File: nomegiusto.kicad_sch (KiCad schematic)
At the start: 14 parts, among them CN1 Wago connector, CN2 Wago connector, CN3 Wago connector, CN4 Wago connector, CN5 Wago connector, CN6 Wago connector, J20 Conn_01x03, J21 Conn_01x03

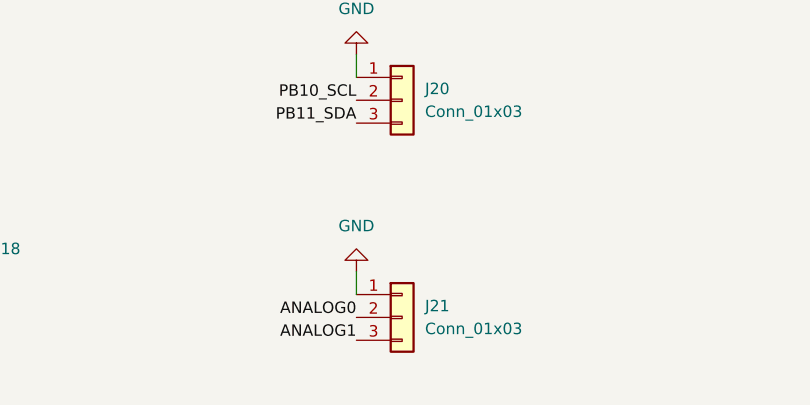
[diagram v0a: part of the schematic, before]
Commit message: changed IMU, reworked PCB layout
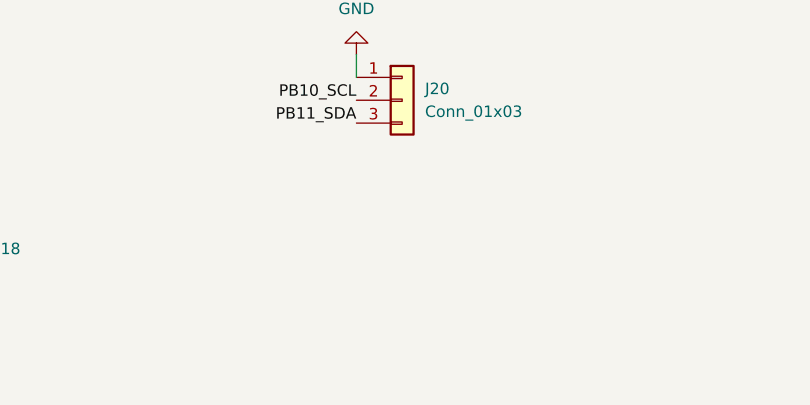
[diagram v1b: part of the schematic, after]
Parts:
- removed J21: Conn_01x03, Connector_PinHeader_2.54mm:PinHeader_1x03_P2.54mm_Vertical, symbol Connector_Generic:Conn_01x03
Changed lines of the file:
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@@
-	(wire
-		(pts
-			(xy 106.68 140.97) (xy 106.68 143.51)
-		)
-		(stroke
-			(width 0)
-			(type default)
-		)
-	)
 	(wire
 		(pts
@@
 		)
 	)
-	(label "ANALOG0"
-		(at 106.68 146.05 180)
-		(effects
-			(font
-				(size 1.27 1.27)
-			)
-			(justify right bottom)
-		)
-	)
 	(label "INPUT6"
 		(at 105.41 52.07 180)
@@
 	(label "PB11_SDA"
 		(at 106.68 124.46 180)
-		(effects
-			(font
-				(size 1.27 1.27)
-			)
-			(justify right bottom)
-		)
-	)
-	(label "ANALOG1"
-		(at 106.68 148.59 180)
 		(effects
 			(font
@@
 					(unit 1)
 				)
-			)
-		)
-	)
-	(symbol
-		(lib_id "power:GND")
-		(at 106.68 140.97 180)
-		(unit 1)
-		(body_style 1)
-		(exclude_from_sim no)
-		(in_bom yes)
-		(on_board yes)
-		(in_pos_files yes)
-		(dnp no)
-		(fields_autoplaced yes)
-		(property "Reference" "#PWR092"
-			(at 106.68 134.62 0)
-			(hide yes)
-			(show_name no)
-			(do_not_autoplace no)
-			(effects
-				(font
-					(size 1.27 1.27)
-				)
-			)
-		)
-		(property "Value" "GND"
-			(at 106.68 135.89 0)
-			(show_name no)
-			(do_not_autoplace no)
-			(effects
-				(font
-					(size 1.27 1.27)
-				)
-			)
-		)
-		(property "Footprint" ""
-			(at 106.68 140.97 0)
-			(hide yes)
-			(show_name no)
-			(do_not_autoplace no)
-			(effects
-				(font
-					(size 1.27 1.27)
-				)
-			)
-		)
-		(property "Datasheet" ""
-			(at 106.68 140.97 0)
-			(hide yes)
-			(show_name no)
-			(do_not_autoplace no)
-			(effects
-				(font
-					(size 1.27 1.27)
-				)
-			)
-		)
-		(property "Description" "Power symbol creates a global label with name \"GND\" , ground"
-			(at 106.68 140.97 0)
-			(hide yes)
-			(show_name no)
-			(do_not_autoplace no)
-			(effects
-				(font
-					(size 1.27 1.27)
-				)
-			)
-		)
-		(pin "1"
-		)
-		(instances
-			(project "pandahat"
-				(path "/e63e39d7-6ac0-4ffd-8aa3-1841a4541b55/9c6aa88d-0a18-4640-97a5-d19b2054e8d0"
-					(reference "#PWR092")
-					(unit 1)
-				)
-			)
-		)
-	)
-	(symbol
-		(lib_id "Connector_Generic:Conn_01x03")
-		(at 111.76 146.05 0)
-		(unit 1)
-		(body_style 1)
-		(exclude_from_sim no)
-		(in_bom yes)
-		(on_board yes)
-		(in_pos_files yes)
-		(dnp no)
-		(fields_autoplaced yes)
-		(property "Reference" "J21"
-			(at 114.3 144.7799 0)
-			(show_name no)
-			(do_not_autoplace no)
-			(effects
-				(font
-					(size 1.27 1.27)
-				)
-				(justify left)
-			)
-		)
-		(property "Value" "Conn_01x03"
-			(at 114.3 147.3199 0)
-			(show_name no)
-			(do_not_autoplace no)
-			(effects
-				(font
-					(size 1.27 1.27)
-				)
-				(justify left)
-			)
-		)
-		(property "Footprint" "Connector_PinHeader_2.54mm:PinHeader_1x03_P2.54mm_Vertical"
-			(at 111.76 146.05 0)
-			(hide yes)
-			(show_name no)
-			(do_not_autoplace no)
-			(effects
-				(font
-					(size 1.27 1.27)
-				)
-			)
-		)
-		(property "Datasheet" ""
-			(at 111.76 146.05 0)
-			(hide yes)
-			(show_name no)
-			(do_not_autoplace no)
-			(effects
-				(font
-					(size 1.27 1.27)
-				)
-			)
-		)
-		(property "Description" "Generic connector, single row, 01x03, script generated (kicad-library-utils/schlib/autogen/connector/)"
-			(at 111.76 146.05 0)
-			(hide yes)
-			(show_name no)
-			(do_not_autoplace no)
-			(effects
-				(font
-					(size 1.27 1.27)
-				)
-			)
-		)
-		(pin "2"
-		)
-		(pin "3"
-		)
-		(pin "1"
-		)
-		(instances
-			(project "pandahat"
-				(path "/e63e39d7-6ac0-4ffd-8aa3-1841a4541b55/9c6aa88d-0a18-4640-97a5-d19b2054e8d0"
-					(reference "J21")
-					(unit 1)
-				)

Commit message: more work
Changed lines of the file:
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@@
 		)
 	)
-	(hierarchical_label "UARTX_RX"
+	(hierarchical_label "UART_RX"
 		(shape input)
 		(at 153.67 24.13 0)

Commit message: Finished pcb
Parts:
- added CN8: JST 4PIN, easyeda2kicad:CONN-TH_B4B-PH-K-S, symbol lol:B4B-PH-K-S
- added R25, R26, R35, R36: 0603WAF1002T5E, easyeda2kicad:R0603, symbol lol:0603WAF1002T5E
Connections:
- net GND: now also CN8.1
- net PB10_SCL renamed IMU_SCL
- net IMU_SCL: now also R26.2
- net PB11_SDA renamed IMU_SDA
- net IMU_SDA: now also R25.2
- new net +3.3V: CN8.4, R25.1, R26.1, R35.1, R36.1
- new net EXTRA_SCL: CN8.3, R36.2
- new net EXTRA_SDA: CN8.2, R35.2
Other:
- added sheet Gpio expose5 (gpio_expose.kicad_sch)
- added sheet Gpio expose6 (gpio_expose.kicad_sch)
- added sheet Gpio expose7 (gpio_expose.kicad_sch)
- added sheet Gpio expose8 (gpio_expose.kicad_sch)
- sheet STM32 ports: added PC13, PC14, PC15, PD0, PD1; removed none
- moved on the sheet: J20
